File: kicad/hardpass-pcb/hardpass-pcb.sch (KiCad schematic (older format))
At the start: 34 parts, among them CON1 ER-OLED-FPC20, P1 Pi_Zero, SW1 1, SW10 C/UP, SW11 0/OK, SW12 OK/DN, SW13 SHUTDN, SW2 2, SW3 3, SW4 4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

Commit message: removed spi labels from oled (won#t happen anyways)
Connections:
- net labels removed: OLED_CS, OLED_DC, OLED_MOSI, OLED_RES, OLED_SCK
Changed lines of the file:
@@
 	1    0    0    -1
 $EndComp
-Text Label 6050 2100 0    60   ~ 0
-OLED_CS
-Text Label 6050 2200 0    60   ~ 0
-OLED_RES
-Text Label 6050 2300 0    60   ~ 0
-OLED_DC
-Text Label 6050 2400 0    60   ~ 0
-OLED_SCK
-Text Label 6050 2500 0    60   ~ 0
-OLED_MOSI
 $Comp
 L C_Small C7

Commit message: removed a few footprint labels for cleaner look
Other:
- note added: "Wifi Pants: \n pin 27-->"
- note removed: "Pins for SPI use"
- note removed: "Wifi Pants: pin 27"
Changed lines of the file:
@@
 F 0 "SW1" H 2050 5110 50  0000 C CNN
 F 1 "1" H 1900 4950 50  0000 C CNN
-F 2 "Buttons_Switches_SMD:SW_SPST_PTS645" H 4650 5450 50  0000 C CNN
+F 2 "Buttons_Switches_SMD:SW_SPST_PTS645" H 2500 3550 50  0000 C CNN
 F 3 "" H 1900 5000 50  0000 C CNN
 	1    1900 5000
@@
 F 0 "SW2" H 2500 5110 50  0000 C CNN
 F 1 "2" H 2350 4950 50  0000 C CNN
-F 2 "Buttons_Switches_SMD:SW_SPST_PTS645" H 4650 5350 50  0000 C CNN
+F 2 "Buttons_Switches_SMD:SW_SPST_PTS645" H 4650 5350 50  0001 C CNN
 F 3 "" H 2350 5000 50  0000 C CNN
 	1    2350 5000
@@
 F 0 "SW3" H 2950 5110 50  0000 C CNN
 F 1 "3" H 2800 4950 50  0000 C CNN
-F 2 "Buttons_Switches_SMD:SW_SPST_PTS645" H 4650 5250 50  0000 C CNN
+F 2 "Buttons_Switches_SMD:SW_SPST_PTS645" H 4650 5250 50  0001 C CNN
 F 3 "" H 2800 5000 50  0000 C CNN
 	1    2800 5000
@@
 F 0 "SW4" H 2050 5510 50  0000 C CNN
 F 1 "4" H 1900 5350 50  0000 C CNN
-F 2 "Buttons_Switches_SMD:SW_SPST_PTS645" H 4650 5950 50  0000 C CNN
+F 2 "Buttons_Switches_SMD:SW_SPST_PTS645" H 4650 5950 50  0001 C CNN
 F 3 "" H 1900 5400 50  0000 C CNN
 	1    1900 5400
@@
 F 0 "SW5" H 2500 5510 50  0000 C CNN
 F 1 "5" H 2350 5350 50  0000 C CNN
-F 2 "Buttons_Switches_SMD:SW_SPST_PTS645" H 4650 5850 50  0000 C CNN
+F 2 "Buttons_Switches_SMD:SW_SPST_PTS645" H 4650 5850 50  0001 C CNN
 F 3 "" H 2350 5400 50  0000 C CNN
 	1    2350 5400
@@
 F 0 "SW6" H 2950 5510 50  0000 C CNN
 F 1 "6" H 2800 5350 50  0000 C CNN
-F 2 "Buttons_Switches_SMD:SW_SPST_PTS645" H 4650 5750 50  0000 C CNN
+F 2 "Buttons_Switches_SMD:SW_SPST_PTS645" H 4650 5750 50  0001 C CNN
 F 3 "" H 2800 5400 50  0000 C CNN
 	1    2800 5400
@@
 F 0 "SW7" H 2050 5910 50  0000 C CNN
 F 1 "7" H 1900 5750 50  0000 C CNN
-F 2 "Buttons_Switches_SMD:SW_SPST_PTS645" H 4650 6450 50  0000 C CNN
+F 2 "Buttons_Switches_SMD:SW_SPST_PTS645" H 4650 6450 50  0001 C CNN
 F 3 "" H 1900 5800 50  0000 C CNN
 	1    1900 5800
@@
 F 0 "SW8" H 2500 5910 50  0000 C CNN
 F 1 "8" H 2350 5750 50  0000 C CNN
-F 2 "Buttons_Switches_SMD:SW_SPST_PTS645" H 4650 6350 50  0000 C CNN
+F 2 "Buttons_Switches_SMD:SW_SPST_PTS645" H 4650 6350 50  0001 C CNN
 F 3 "" H 2350 5800 50  0000 C CNN
 	1    2350 5800
@@
 F 0 "SW9" H 2950 5910 50  0000 C CNN
 F 1 "9" H 2800 5750 50  0000 C CNN
-F 2 "Buttons_Switches_SMD:SW_SPST_PTS645" H 4650 6250 50  0000 C CNN
+F 2 "Buttons_Switches_SMD:SW_SPST_PTS645" H 4650 6250 50  0001 C CNN
 F 3 "" H 2800 5800 50  0000 C CNN
 	1    2800 5800
@@
 F 0 "SW10" H 2050 6310 50  0000 C CNN
 F 1 "C/UP" H 1800 6150 50  0000 C CNN
-F 2 "Buttons_Switches_SMD:SW_SPST_PTS645" H 4650 6950 50  0000 C CNN
+F 2 "Buttons_Switches_SMD:SW_SPST_PTS645" H 4650 6950 50  0001 C CNN
 F 3 "" H 1900 6200 50  0000 C CNN
 	1    1900 6200
@@
 F 0 "SW11" H 2500 6310 50  0000 C CNN
 F 1 "0/OK" H 2250 6150 50  0000 C CNN
-F 2 "Buttons_Switches_SMD:SW_SPST_PTS645" H 4650 6850 50  0000 C CNN
+F 2 "Buttons_Switches_SMD:SW_SPST_PTS645" H 4650 6850 50  0001 C CNN
 F 3 "" H 2350 6200 50  0000 C CNN
 	1    2350 6200
@@
 F 0 "SW12" H 2950 6310 50  0000 C CNN
 F 1 "OK/DN" H 2700 6150 50  0000 C CNN
-F 2 "Buttons_Switches_SMD:SW_SPST_PTS645" H 4650 6750 50  0000 C CNN
+F 2 "Buttons_Switches_SMD:SW_SPST_PTS645" H 4650 6750 50  0001 C CNN
 F 3 "" H 2800 6200 50  0000 C CNN
 	1    2800 6200
@@
 F 0 "C6" V 6000 1350 50  0000 L CNN
 F 1 "1µF" H 5950 1150 50  0000 L CNN
-F 2 "Capacitors_SMD:C_1206" V 5950 2800 50  0000 C CNN
+F 2 "Capacitors_SMD:C_1206" V 5800 550 50  0000 C CNN
 F 3 "" H 5950 1300 50  0000 C CNN
 	1    5950 1300
@@
 F 0 "C5" V 6000 1550 50  0000 L CNN
 F 1 "1µF" H 5950 1350 50  0000 L CNN
-F 2 "Capacitors_SMD:C_1206" V 5950 3000 50  0000 C CNN
+F 2 "Capacitors_SMD:C_1206" V 5950 3000 50  0001 C CNN
 F 3 "" H 5950 1500 50  0000 C CNN
 	1    5950 1500
@@
 F 0 "C1" V 5800 1950 50  0000 L CNN
 F 1 "1µF" V 5700 1700 50  0000 L CNN
-F 2 "Capacitors_SMD:C_1206" V 5750 200 50  0000 C CNN
+F 2 "Capacitors_SMD:C_1206" V 5750 200 50  0001 C CNN
 F 3 "" H 5750 1900 50  0000 C CNN
 	1    5750 1900
@@
 F 0 "C2" V 5450 1750 50  0000 L CNN
 F 1 "1µF" V 5350 1500 50  0000 L CNN
-F 2 "Capacitors_SMD:C_1206" V 5400 -350 50  0000 C CNN
+F 2 "Capacitors_SMD:C_1206" V 5400 -350 50  0001 C CNN
 F 3 "" H 5400 1700 50  0000 C CNN
 	1    5400 1700
@@
 F 0 "C3" V 6000 2850 50  0000 L CNN
 F 1 "2.2µF" V 6000 2550 50  0000 L CNN
-F 2 "Capacitors_SMD:C_1206" V 5950 4300 50  0000 C CNN
+F 2 "Capacitors_SMD:C_1206" V 5950 4300 50  0001 C CNN
 F 3 "" H 5950 2800 50  0000 C CNN
 	1    5950 2800
@@
 F 0 "C4" V 6000 2750 50  0000 L CNN
 F 1 "4.7µF" V 6000 2450 50  0000 L CNN
-F 2 "Capacitors_SMD:C_1206" V 5950 4200 50  0000 C CNN
+F 2 "Capacitors_SMD:C_1206" V 5950 4200 50  0001 C CNN
 F 3 "" H 5950 2700 50  0000 C CNN
 	1    5950 2700
@@
 F 0 "R1" V 6000 2700 50  0000 L CNN
 F 1 "390k" V 6000 2350 50  0000 L CNN
-F 2 "Resistors_SMD:R_1206" V 5950 4100 50  0000 C CNN
+F 2 "Resistors_SMD:R_1206" V 5950 4100 50  0001 C CNN
 F 3 "" H 5950 2600 50  0000 C CNN
 	1    5950 2600
@@
 F 0 "R11" V 5850 2550 50  0000 L CNN
 F 1 "10k" V 5850 2200 50  0000 L CNN
-F 2 "Resistors_SMD:R_1206" V 5850 4050 50  0000 C CNN
+F 2 "Resistors_SMD:R_1206" V 5850 4050 50  0001 C CNN
 F 3 "" H 5850 2450 50  0000 C CNN
 	1    5850 2450
@@
 F 0 "R10" V 5850 2450 50  0000 L CNN
 F 1 "10k" V 5850 2100 50  0000 L CNN
-F 2 "Resistors_SMD:R_1206" V 5850 3950 50  0000 C CNN
+F 2 "Resistors_SMD:R_1206" V 4750 1700 50  0000 C CNN
 F 3 "" H 5850 2350 50  0000 C CNN
 	1    5850 2350
@@
 	1    0    0    -1
 $EndComp
-Text Notes 6650 2600 1    60   ~ 0
-Pins for SPI use
-Text Notes 350  1450 0    60   ~ 0
-Wifi Pants: pin 27
+Text Notes 500  1450 0    60   ~ 0
+Wifi Pants: \n    pin 27-->
 $Comp
 L GND #PWR09
@@
 F 0 "C7" H 4900 2150 50  0000 L CNN
 F 1 "0.1µF" H 4600 2150 50  0000 L CNN
-F 2 "Capacitors_SMD:C_1206" H 7450 2200 50  0000 C CNN
+F 2 "Capacitors_SMD:C_1206" H 7450 2200 50  0001 C CNN
 F 3 "" H 4850 2200 50  0000 C CNN
 	1    4850 2200
@@
 F 0 "R2" V 4750 1950 50  0000 L CNN
 F 1 "100k" V 4950 1900 50  0000 L CNN
-F 2 "Resistors_SMD:R_1206" H 2250 2000 50  0000 C CNN
+F 2 "Resistors_SMD:R_1206" H 2250 2000 50  0001 C CNN
 F 3 "" H 4850 2000 50  0000 C CNN
 	1    4850 2000
@@
 F 0 "R3" V 5200 2100 50  0000 L CNN
 F 1 "100k" V 5000 2050 50  0000 L CNN
-F 2 "Resistors_SMD:R_1206" V 5100 4450 50  0000 C CNN
+F 2 "Resistors_SMD:R_1206" V 5100 4450 50  0001 C CNN
 F 3 "" H 5100 2100 50  0000 C CNN
 	1    5100 2100
@@
 F 0 "R12" H 8450 5400 50  0000 L CNN
 F 1 "33" V 8500 5250 50  0000 L CNN
-F 2 "Resistors_SMD:R_1206" V 7800 5200 50  0000 C CNN
+F 2 "Resistors_SMD:R_1206" V 7800 5200 50  0001 C CNN
 F 3 "" H 8500 5300 50  0000 C CNN
 	1    8500 5300
@@
 F 0 "R13" H 8550 5400 50  0000 L CNN
 F 1 "33" V 8600 5250 50  0000 L CNN
-F 2 "Resistors_SMD:R_1206" V 7900 5200 50  0000 C CNN
+F 2 "Resistors_SMD:R_1206" V 7900 5200 50  0001 C CNN
 F 3 "" H 8600 5300 50  0000 C CNN
 	1    8600 5300
@@
 F 0 "R14" H 8650 5400 50  0000 L CNN
 F 1 "33" V 8700 5250 50  0000 L CNN
-F 2 "Resistors_SMD:R_1206" V 8000 5200 50  0000 C CNN
+F 2 "Resistors_SMD:R_1206" V 8000 5200 50  0001 C CNN
 F 3 "" H 8700 5300 50  0000 C CNN
 	1    8700 5300
@@
 F 0 "R15" H 8750 5400 50  0000 L CNN
 F 1 "33" V 8800 5250 50  0000 L CNN
-F 2 "Resistors_SMD:R_1206" V 8100 5200 50  0000 C CNN
+F 2 "Resistors_SMD:R_1206" V 8100 5200 50  0001 C CNN
 F 3 "" H 8800 5300 50  0000 C CNN
 	1    8800 5300
@@
 F 0 "R16" H 8850 5400 50  0000 L CNN
 F 1 "33" V 8900 5250 50  0000 L CNN
-F 2 "Resistors_SMD:R_1206" V 8200 5200 50  0000 C CNN
+F 2 "Resistors_SMD:R_1206" V 8200 5200 50  0001 C CNN
 F 3 "" H 8900 5300 50  0000 C CNN
 	1    8900 5300

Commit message: re-done pcb for 30 pin oled
pcb was completely redone, fixing header-misalignment (hopefully) and removing ugly silk screen from the front
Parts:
- removed CON1: ER-OLED-FPC20, hardpass:Solderpads_OLED20Pin_.5mmPitch, symbol ER-OLED-FPC20
- added P2: OLED_I2C, adafruit-oled:UG-2864HSWEG01_0.96IN_WRAPAROUND, symbol CONN_01X30
- P1: footprint hardpass:Pin_Header_Mirrored-NoHoles_2x20 -> hardpass:Pin_Header_Mirrored-NoHoles_centered_2x20
- SW1, SW10, SW11, SW12, SW2, SW3, SW4, SW5, SW6, SW7, SW8, SW9: footprint Buttons_Switches_SMD:SW_SPST_PTS645 -> hardpass:SW_SPST_PTS645_nosilk
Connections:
- wire segments 46 -> 53
- no-connect marks 15 -> 16
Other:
- note added: "Switching to SPI4:\n - pull 11 down\n - disconnect 20"
- moved on the sheet: C2, C3, C4, C5, C6, C7, R1, R10, R11, R2, R3

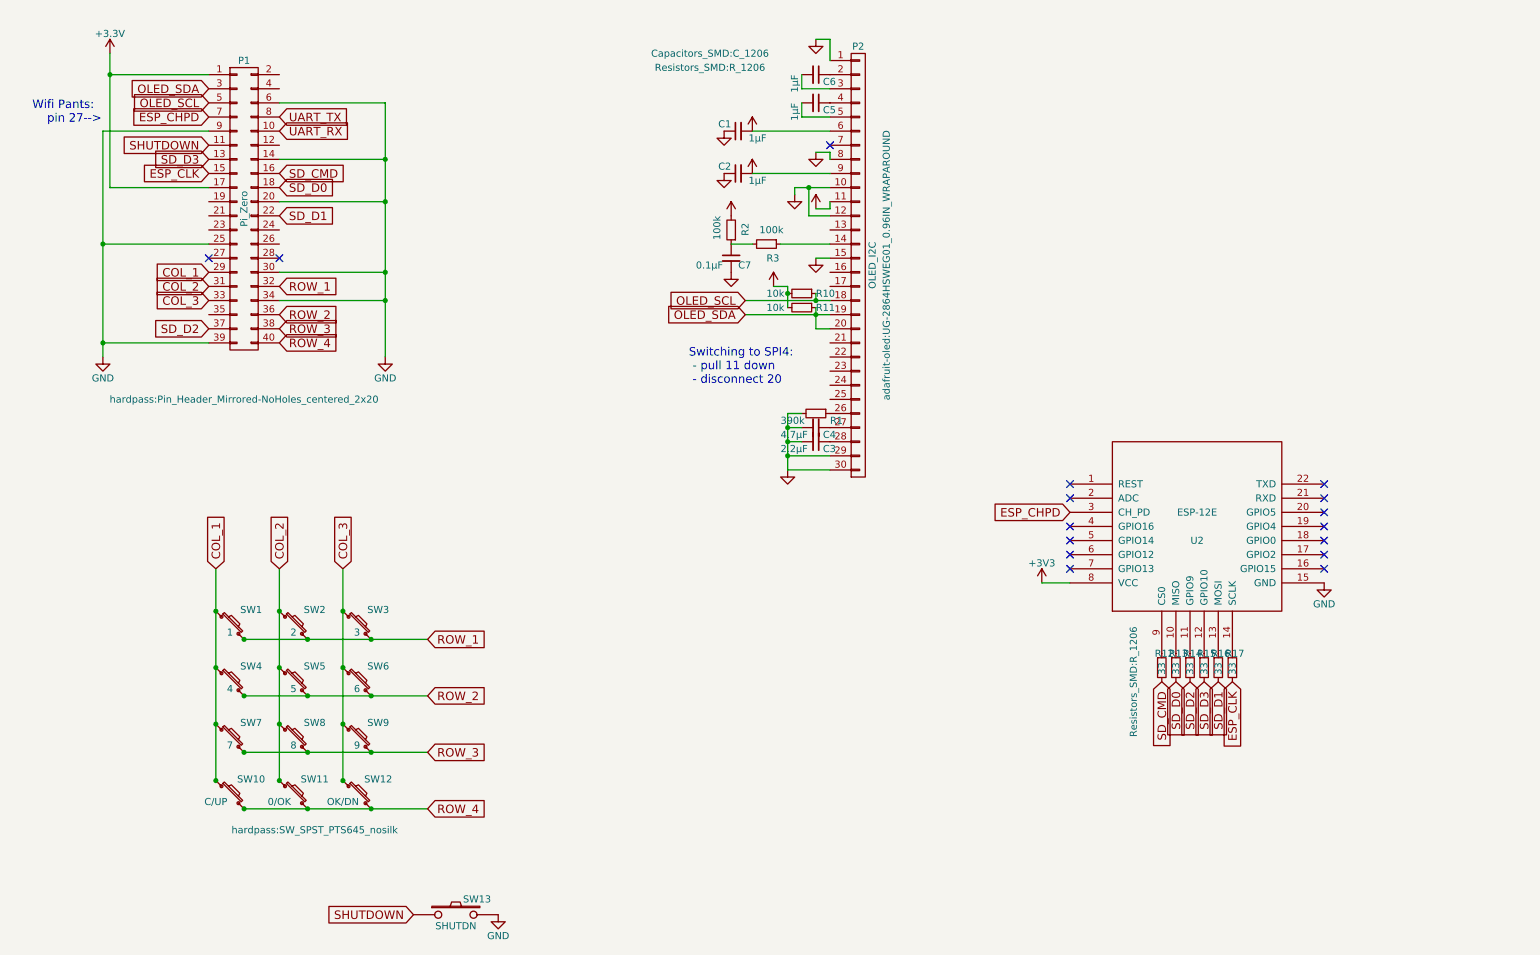
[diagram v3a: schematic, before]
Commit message: wired up tda8029
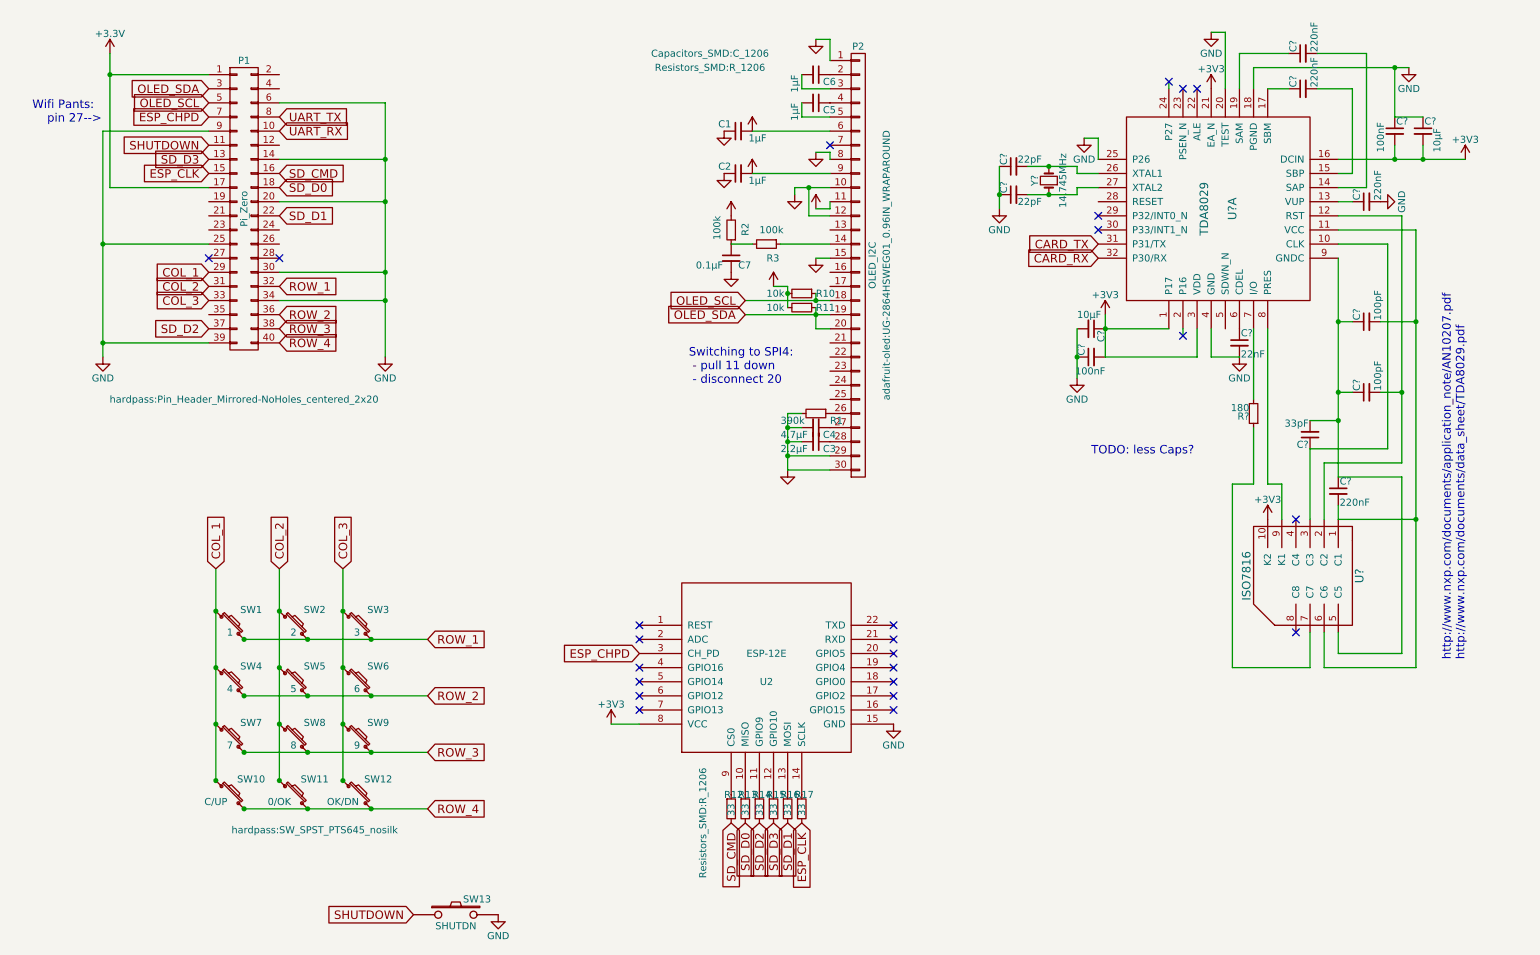
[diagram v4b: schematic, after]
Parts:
- added C? (x2): 22pF, symbol C_Small
- added C? (x4): 220nF, symbol C_Small
- added C? (x2): 100nF, symbol C_Small
- added C? (x2): 10µF, symbol C_Small
- added C? (x2): 100pF, symbol C_Small
- added C?: 22nF, symbol C_Small
- added C?: 33pF, symbol C_Small
- added R?: 180, symbol R_Small
- added U?: TDA8029, symbol TDA8029
- added U?: ISO7816, symbol ISO7816
- added Y?: 14.745MHz, symbol Crystal_Small
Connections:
- net +3V3: now also C?.1, C?.2, C?.2, C?.2, U?.1 (P17), U?.10 (K2), U?.16 (DCIN), U?.21 (EA_N), U?.3 (VDD)
- net GND: now also C?.1, C?.1, C?.1, C?.1, C?.1, C?.2, C?.2, C?.2, U?.18 (PGND), U?.20 (TEST), U?.25 (P26), U?.4 (GND)
- new net: C?.1, U?.10 (CLK), U?.3 (C3)
- new net: C?.2, C?.2, U?.1 (C1), U?.11 (VCC), U?.6 (C6)
- new net: C?.2, U?.12 (RST), U?.2 (C2)
- new net: C?.1, U?.13 (VUP)
- new net: C?.2, U?.14 (SAP)
- new net: C?.2, U?.15 (SBP)
- new net: C?.1, U?.17 (SBM)
- new net: C?.1, U?.19 (SAM)
- new net: C?.2, U?.26 (XTAL1), Y?.2
- new net: C?.2, U?.27 (XTAL2), Y?.1
- new net: C?.1, U?.6 (CDEL)
- new net: R?.2, U?.7 (I/O)
- new net: U?.8 (PRES), U?.9 (K1)
- new net: C?.1, C?.1, C?.1, C?.2, U?.5 (C5), U?.9 (GNDC)
- new net: R?.1, U?.7 (C7)
- new net CARD_RX: U?.32 (P30/RX)
- new net CARD_TX: U?.31 (P31/TX)
- no-connect marks 16 -> 24
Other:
- note added: "TODO: less Caps?"
- note added: "http://www.nxp.com/documents/application_note/AN10207.pdf\nhttp://www.nxp.com/documents/data_sheet/TDA8029.pdf"
- moved on the sheet: R12, R13, R14, R15, R16, R17, U2

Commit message: moving stuff around the tda8029
rotated schema back to normal
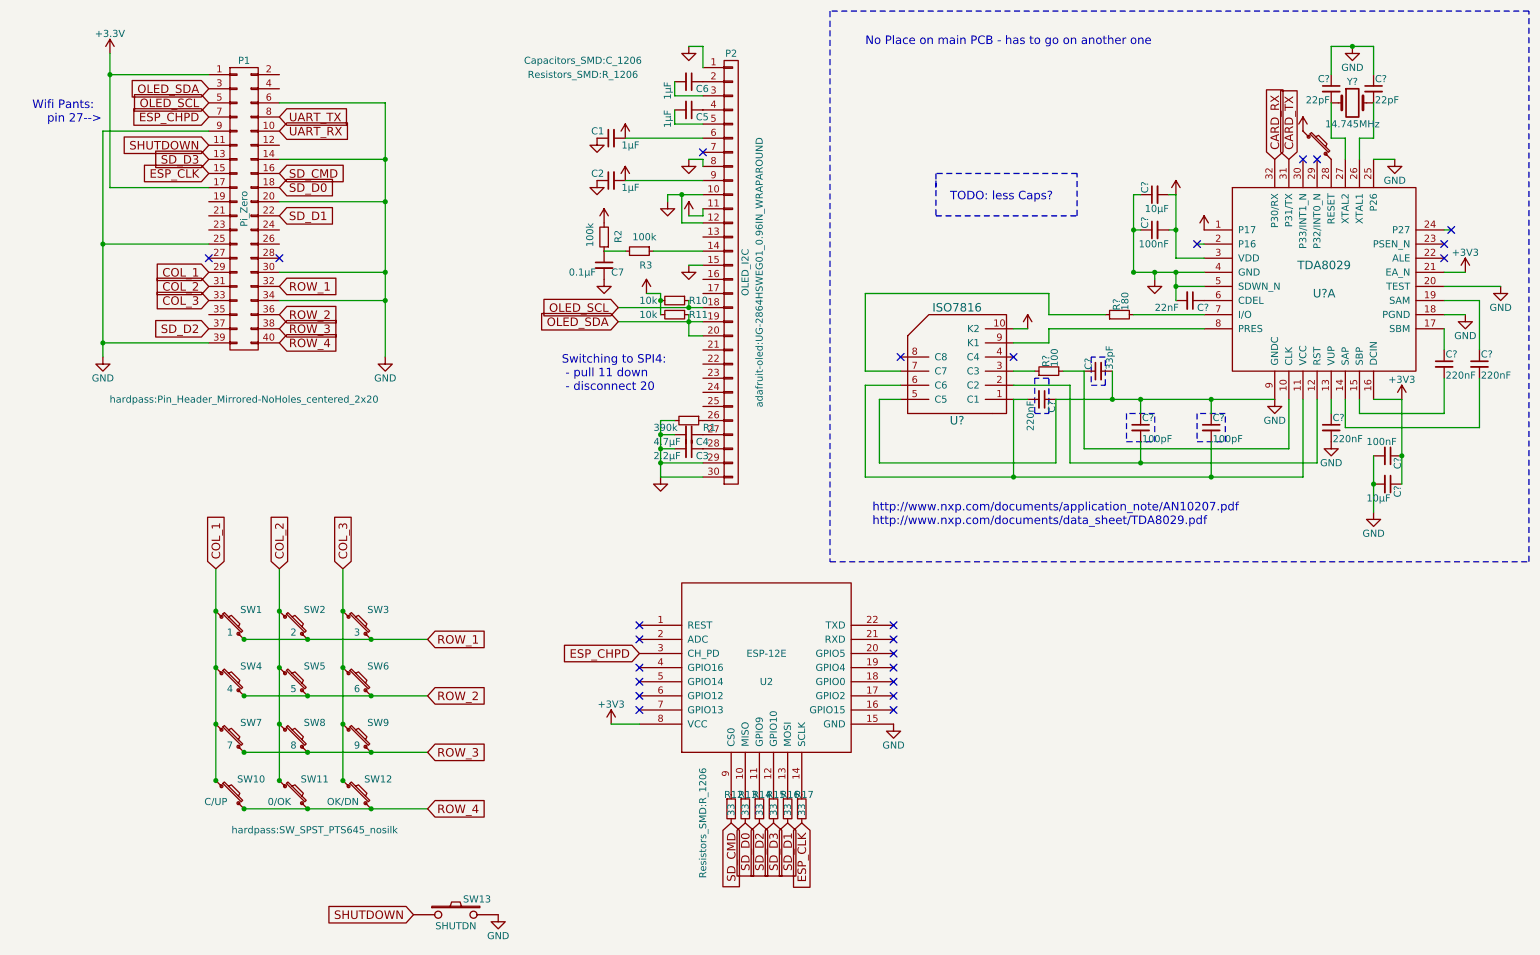
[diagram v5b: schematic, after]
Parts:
- removed C? (x2): 22pF, symbol C_Small
- removed Y?: 14.745MHz, symbol Crystal_Small
- added C? (x2): 22pF, symbol C_Small
- added R?: 100, symbol R_Small
- added SW?: SW_PUSH_SMALL, symbol SW_PUSH_SMALL
- added Y?: 14.745MHz, symbol Crystal
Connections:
- net +3V3: now also C?.1, C?.1, C?.2, SW?.1; no longer C?.1, C?.2, C?.2
- net GND: now also C?.1, C?.1, C?.1, C?.1, C?.2, C?.2, C?.2, U?.5 (C5), U?.5 (SDWN_N), U?.9 (GNDC), C?.1, C?.1; no longer C?.1, C?.1, C?.2
- net at C?.1, U?.10 (CLK): now also R?.2; no longer U?.3 (C3)
- net at U?.26 (XTAL1): now also C?.2, Y?.2
- net at U?.27 (XTAL2): now also C?.2, Y?.1
- net at U?.28 (RESET): now also SW?.2
- new net: R?.1, U?.3 (C3)
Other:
- note added: "No Place on main PCB - has to go on another one"
- moved on the sheet: C1, C2, C3, C4, C5, C6, C7, C?, P2, R1, R10, R11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

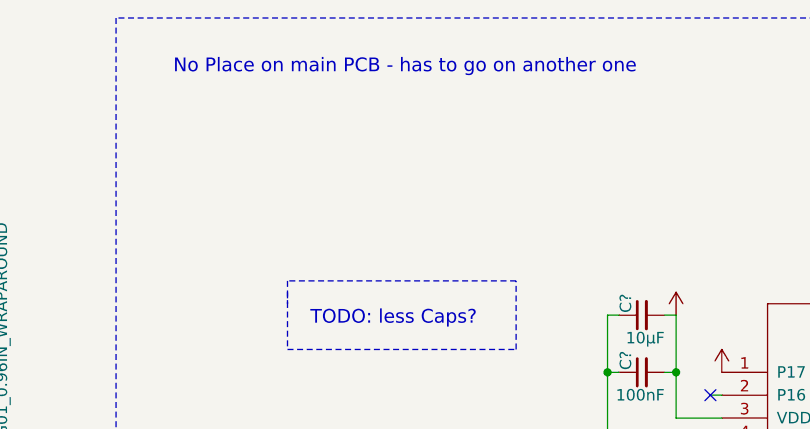
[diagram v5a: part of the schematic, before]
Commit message: added note to schema
possible driver to use with the tda
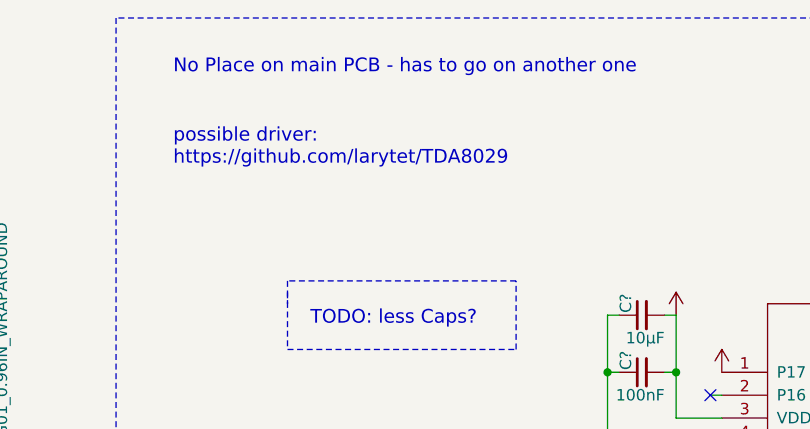
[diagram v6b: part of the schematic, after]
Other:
- note added: "possible driver:\nhttps://github.com/larytet/TDA8029"
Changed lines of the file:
@@
 Wire Wire Line
 	8300 1950 8300 2500
+Text Notes 6400 1300 0    60   ~ 0
+possible driver:\nhttps://github.com/larytet/TDA8029
 $EndSCHEMATC
